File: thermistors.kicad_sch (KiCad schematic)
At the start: 5 parts, among them J3 THERM_1, J4 THERM_2

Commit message: *: Update to kicad 9.0.0
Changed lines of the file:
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@@
 (kicad_sch
-	(version 20231120)
+	(version 20250114)
 	(generator "eeschema")
-	(generator_version "8.0")
+	(generator_version "9.0")
 	(paper "A4")
 	(title_block
@@
 		(at 116.84 73.66)
 		(size 16.51 7.62)
+		(exclude_from_sim no)
+		(in_bom yes)
+		(on_board yes)
+		(dnp no)
 		(stroke
 			(width 0.1524)
@@
 		(at 116.84 88.9)
 		(size 16.51 7.62)
+		(exclude_from_sim no)
+		(in_bom yes)
+		(on_board yes)
+		(dnp no)
 		(stroke
 			(width 0.1524)
@@
 		(at 116.84 96.52)
 		(size 16.51 7.62)
+		(exclude_from_sim no)
+		(in_bom yes)
+		(on_board yes)
+		(dnp no)
 		(stroke
 			(width 0.1524)
@@
 		(at 116.84 81.28)
 		(size 16.51 7.62)
+		(exclude_from_sim no)
+		(in_bom yes)
+		(on_board yes)
+		(dnp no)
 		(stroke
 			(width 0.1524)
@@
 		(at 116.84 104.14)
 		(size 16.51 7.62)
+		(exclude_from_sim no)
+		(in_bom yes)
+		(on_board yes)
+		(dnp no)
 		(stroke
 			(width 0.1524)
@@
 		(at 116.84 58.42)
 		(size 16.51 7.62)
+		(exclude_from_sim no)
+		(in_bom yes)
+		(on_board yes)
+		(dnp no)
 		(stroke
 			(width 0.1524)
@@
 		(at 40.64 31.75)
 		(size 16.51 38.1)
+		(exclude_from_sim no)
+		(in_bom yes)
+		(on_board yes)
+		(dnp no)
 		(fields_autoplaced yes)
 		(stroke
@@
 		(at 116.84 66.04)
 		(size 16.51 7.62)
+		(exclude_from_sim no)
+		(in_bom yes)
+		(on_board yes)
+		(dnp no)
 		(stroke
 			(width 0.1524)

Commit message: *: Fix whitespace in BOM
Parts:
- TH1, TH2, TH3: Mfr Sunlord -> Sunlord
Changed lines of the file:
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@@
 			)
 		)
-		(property "Mfr" " Sunlord"
+		(property "Mfr" "Sunlord"
 			(at 60.96 63.5 0)
 			(effects
@@
 			)
 		)
-		(property "Mfr" " Sunlord"
+		(property "Mfr" "Sunlord"
 			(at 60.96 50.8 0)
 			(effects
@@
 			)
 		)
-		(property "Mfr" " Sunlord"
+		(property "Mfr" "Sunlord"
 			(at 60.96 38.1 0)
 			(effects

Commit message: bom: Update incorrect on-board thermistor part number
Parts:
- TH1, TH2, TH3: Dist # C525660 -> C13564; Mfr Sunlord -> Murata; Mfr # SDNT1608X103F3435FTF -> NCP18XH103F03RB
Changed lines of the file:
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@@
 			)
 		)
-		(property "Dist #" "C525660"
+		(property "Dist #" "C13564"
 			(at 60.96 63.5 0)
 			(effects
@@
 			)
 		)
-		(property "Mfr" "Sunlord"
+		(property "Mfr" "Murata"
 			(at 60.96 63.5 0)
 			(effects
@@
 			)
 		)
-		(property "Mfr #" "SDNT1608X103F3435FTF"
+		(property "Mfr #" "NCP18XH103F03RB"
 			(at 60.96 63.5 0)
 			(effects
@@
 			)
 		)
-		(property "Dist #" "C525660"
-			(at 60.96 50.8 0)
-			(effects
-				(font
-					(size 1.27 1.27)
-				)
-				(hide yes)
-			)
-		)
-		(property "Mfr" "Sunlord"
-			(at 60.96 50.8 0)
-			(effects
-				(font
-					(size 1.27 1.27)
-				)
-				(hide yes)
-			)
-		)
-		(property "Mfr #" "SDNT1608X103F3435FTF"
+		(property "Dist #" "C13564"
+			(at 60.96 50.8 0)
+			(effects
+				(font
+					(size 1.27 1.27)
+				)
+				(hide yes)
+			)
+		)
+		(property "Mfr" "Murata"
+			(at 60.96 50.8 0)
+			(effects
+				(font
+					(size 1.27 1.27)
+				)
+				(hide yes)
+			)
+		)
+		(property "Mfr #" "NCP18XH103F03RB"
 			(at 60.96 50.8 0)
 			(effects
@@
 			)
 		)
-		(property "Dist #" "C525660"
+		(property "Dist #" "C13564"
 			(at 60.96 38.1 0)
 			(effects
@@
 			)
 		)
-		(property "Mfr" "Sunlord"
+		(property "Mfr" "Murata"
 			(at 60.96 38.1 0)
 			(effects
@@
 			)
 		)
-		(property "Mfr #" "SDNT1608X103F3435FTF"
+		(property "Mfr #" "NCP18XH103F03RB"
 			(at 60.96 38.1 0)
 			(effects

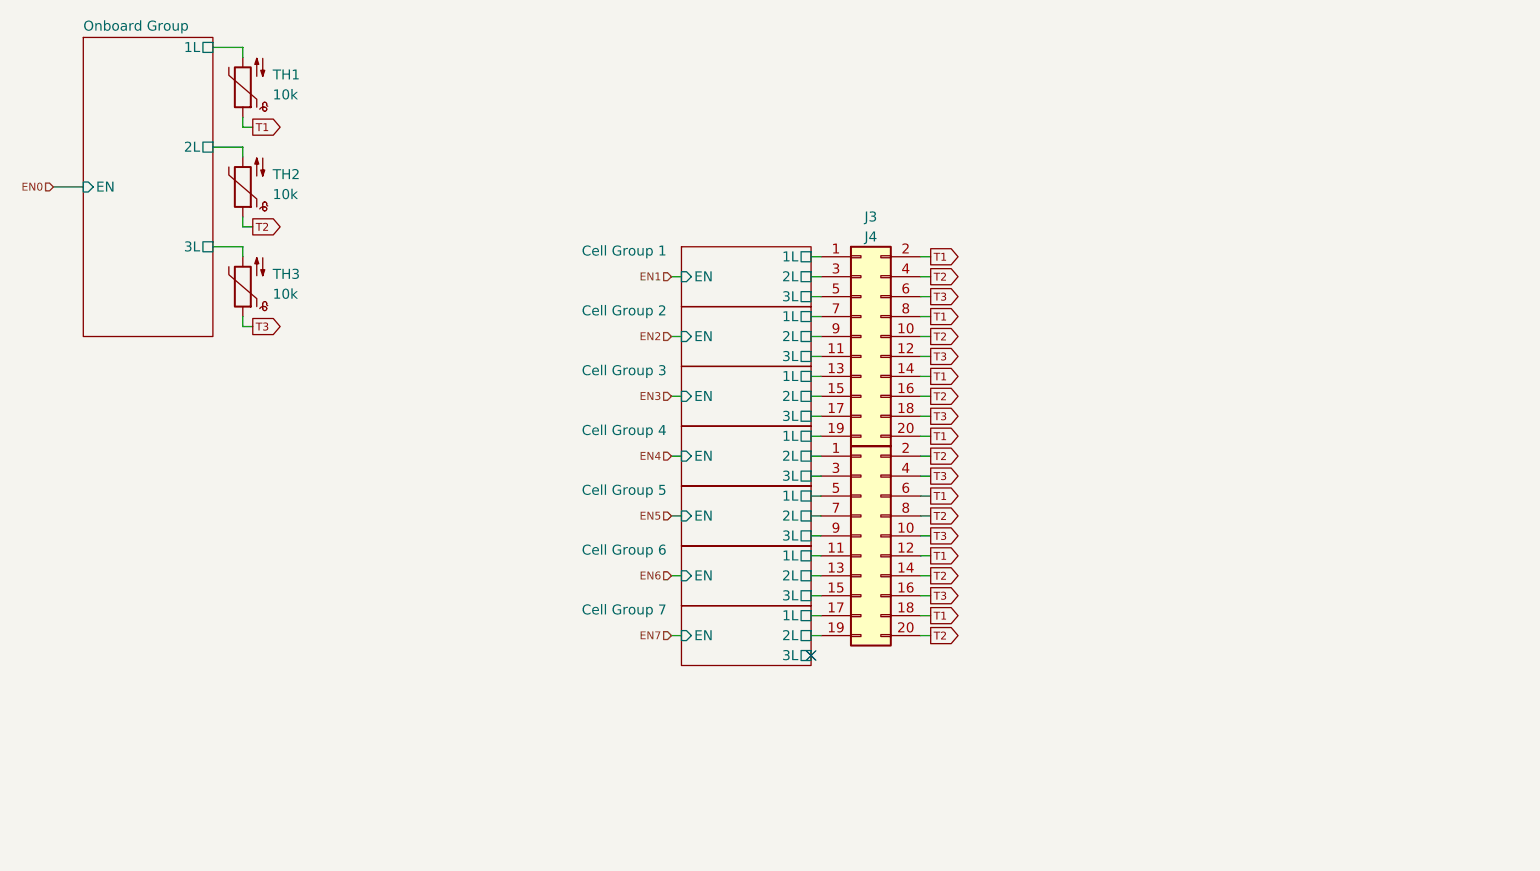
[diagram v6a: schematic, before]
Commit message: *: Use a GPIO expander for the thermistors
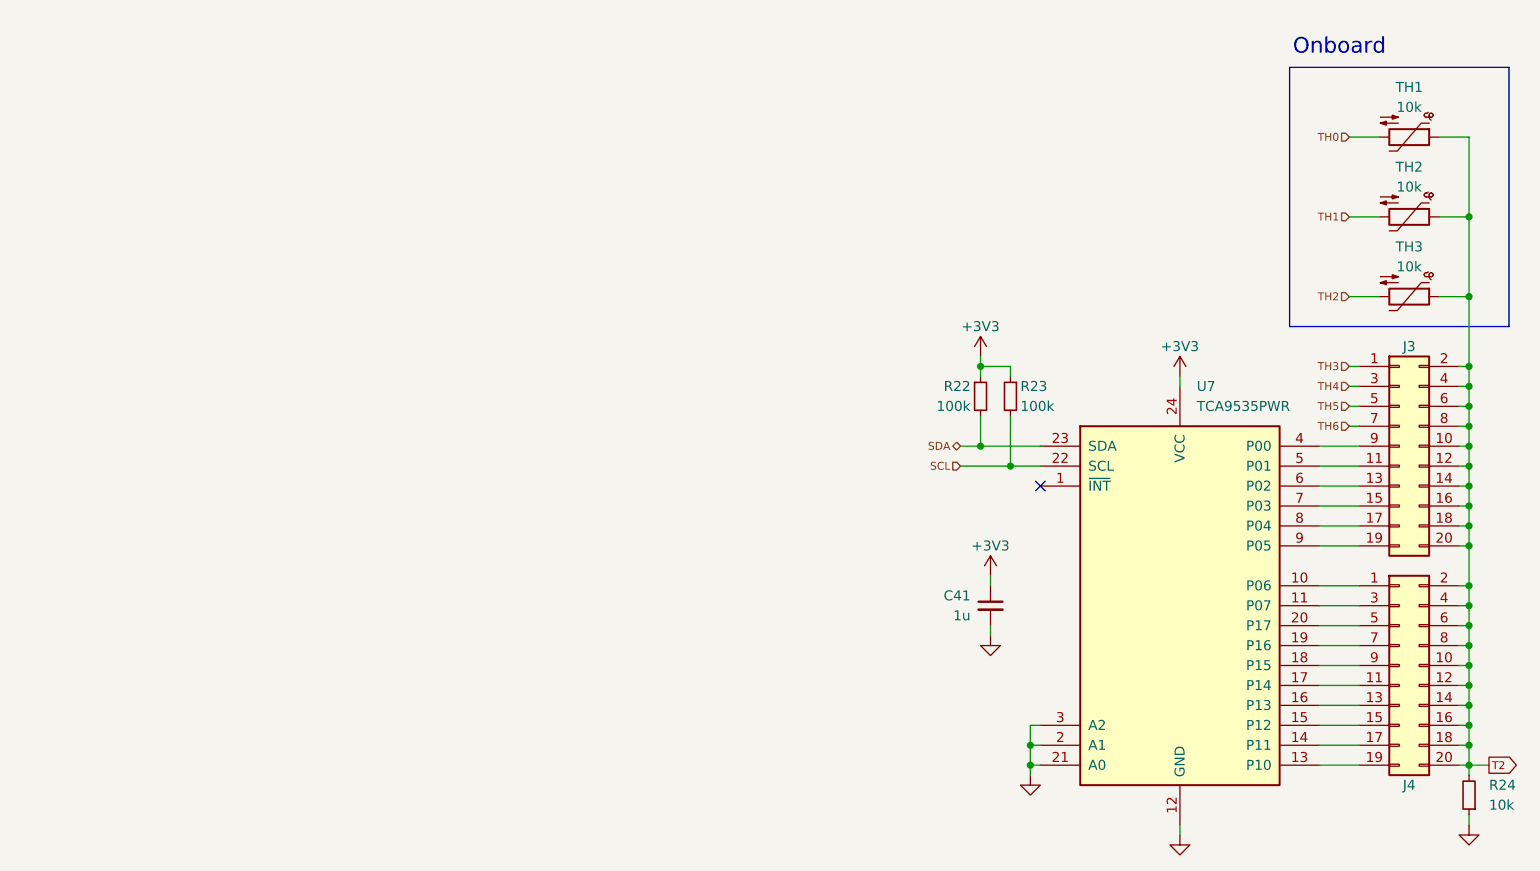
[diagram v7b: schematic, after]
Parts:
- added C41: 1u, Capacitor_SMD:C_0603_1608Metric, symbol Device:C_Small
- added R22, R23: 100k, Resistor_SMD:R_0603_1608Metric, symbol Device:R_Small
- added R24: 10k, Resistor_SMD:R_0603_1608Metric, symbol Device:R_Small
- added U7: TCA9535PWR, Package_SO:TSSOP-24_4.4x7.8mm_P0.65mm, symbol Interface_Expansion:TCA9535PWR
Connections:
- net T1 is gone; now on net T2: J3.14 (Pin_14), J3.2 (Pin_2), J3.20 (Pin_20), J3.8 (Pin_8), J4.12 (Pin_12), J4.18 (Pin_18), J4.6 (Pin_6), TH1.1
- net T3 is gone; now on net T2: J3.12 (Pin_12), J3.18 (Pin_18), J3.6 (Pin_6), J4.10 (Pin_10), J4.16 (Pin_16), J4.4 (Pin_4), TH3.1
- net T2: now also R24.2
- net Cell Group 1/1L renamed TH3
- net Cell Group 1/2L renamed TH4
- net Cell Group 1/3L renamed TH5
- net Cell Group 2/1L renamed TH6
- net Cell Group 2/2L: no longer names the net of J3.9 (Pin_9)
- net Cell Group 2/2L: now also U7.4 (P00)
- net Cell Group 2/3L: no longer names the net of J3.11 (Pin_11)
- net Cell Group 2/3L: now also U7.5 (P01)
- net Cell Group 3/1L: no longer names the net of J3.13 (Pin_13)
- net Cell Group 3/1L: now also U7.6 (P02)
- net Cell Group 3/2L: no longer names the net of J3.15 (Pin_15)
- net Cell Group 3/2L: now also U7.7 (P03)
- net Cell Group 3/3L: no longer names the net of J3.17 (Pin_17)
- net Cell Group 3/3L: now also U7.8 (P04)
- net Cell Group 4/1L: no longer names the net of J3.19 (Pin_19)
- net Cell Group 4/1L: now also U7.9 (P05)
- net Cell Group 4/2L: no longer names the net of J4.1 (Pin_1)
- net Cell Group 4/2L: now also U7.10 (P06)
- net Cell Group 4/3L: no longer names the net of J4.3 (Pin_3)
- net Cell Group 4/3L: now also U7.11 (P07)
- net Cell Group 5/1L: no longer names the net of J4.5 (Pin_5)
- net Cell Group 5/1L: now also U7.20 (P17)
- net Cell Group 5/2L: no longer names the net of J4.7 (Pin_7)
- net Cell Group 5/2L: now also U7.19 (P16)
- net Cell Group 5/3L: no longer names the net of J4.9 (Pin_9)
- net Cell Group 5/3L: now also U7.18 (P15)
- net Cell Group 6/1L: no longer names the net of J4.11 (Pin_11)
- net Cell Group 6/1L: now also U7.17 (P14)
- net Cell Group 6/2L: no longer names the net of J4.13 (Pin_13)
- net Cell Group 6/2L: now also U7.16 (P13)
- net Cell Group 6/3L: no longer names the net of J4.15 (Pin_15)
- net Cell Group 6/3L: now also U7.15 (P12)
- net Cell Group 7/1L: no longer names the net of J4.17 (Pin_17)
- net Cell Group 7/1L: now also U7.14 (P11)
- net Cell Group 7/2L: no longer names the net of J4.19 (Pin_19)
- net Cell Group 7/2L: now also U7.13 (P10)
- net Onboard Group/1L renamed TH0
- net Onboard Group/2L renamed TH1
- net Onboard Group/3L renamed TH2
- new net +3V3: C41.1, R22.1, R23.1, U7.24 (VCC)
- new net GND: C41.2, R24.1, U7.12 (GND), U7.2 (A1), U7.21 (A0), U7.3 (A2)
- new net SCL: R23.2, U7.22 (SCL)
- new net SDA: R22.2, U7.23 (SDA)
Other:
- removed sheet Cell Group 1
- removed sheet Cell Group 2
- removed sheet Cell Group 3
- removed sheet Cell Group 4
- removed sheet Cell Group 5
- removed sheet Cell Group 6
- removed sheet Cell Group 7
- removed sheet Onboard Group
- note added: "Onboard"
- moved on the sheet: J3, J4, TH1, TH2, TH3
